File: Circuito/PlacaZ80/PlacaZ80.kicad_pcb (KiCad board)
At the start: 2 copper layers, 132.1 x 99.1 mm, 32 parts, among them J1 Conn_01x04_Pin, J2 Conn_01x14_Socket, U1 74HC00, U2 74HC138, U3 74LS08, U4 DS1233-05, U5 74HC02, U6 Z80CPU, U7 28C16, U8 6116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

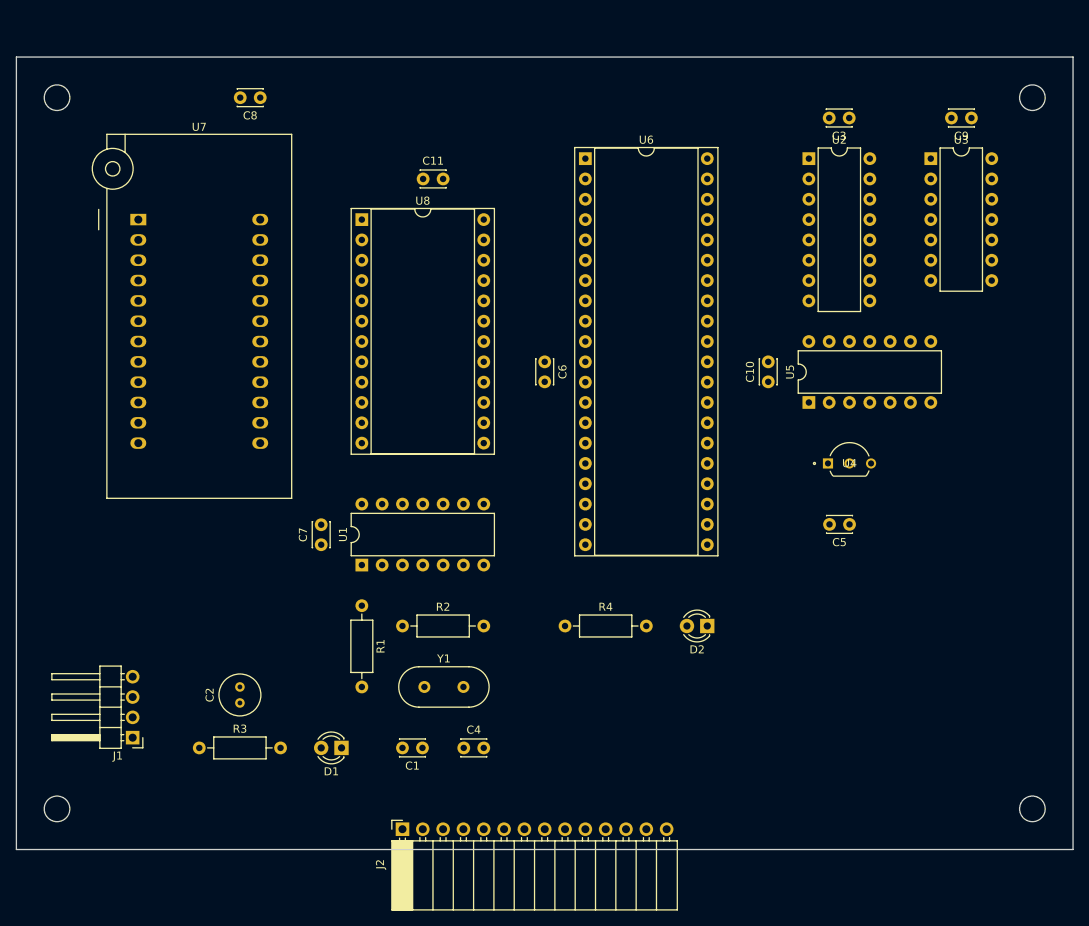
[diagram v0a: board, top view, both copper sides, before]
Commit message: Acréscimo da Placa de IO e o teste do Display
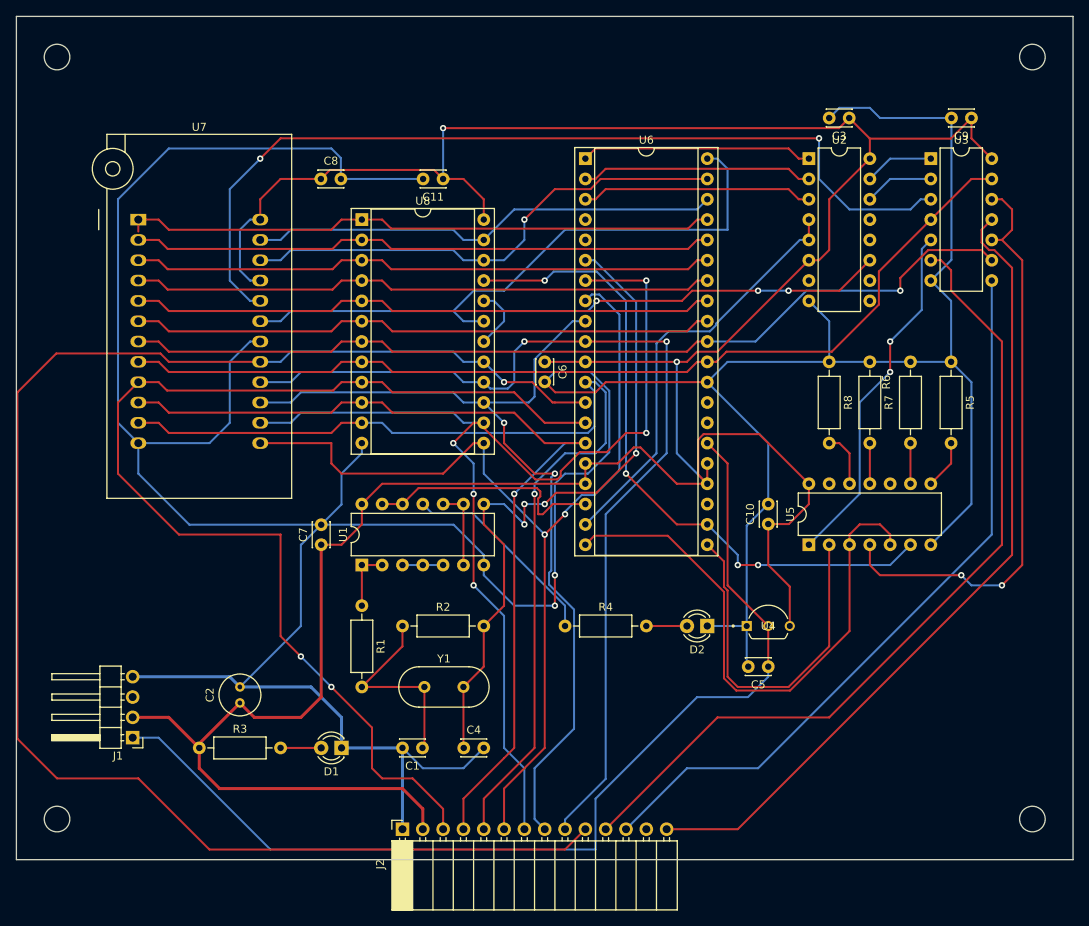
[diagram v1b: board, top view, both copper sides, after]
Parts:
- added R5: 1k, Resistor_THT:R_Axial_DIN0207_L6.3mm_D2.5mm_P10.16mm_Horizontal, F.Cu at (134.6, 58.4)
- added R6: 1k, Resistor_THT:R_Axial_DIN0207_L6.3mm_D2.5mm_P10.16mm_Horizontal, F.Cu at (129.5, 58.4)
- added R7: 1k, Resistor_THT:R_Axial_DIN0207_L6.3mm_D2.5mm_P10.16mm_Horizontal, F.Cu at (124.5, 58.4)
- added R8: 1k, Resistor_THT:R_Axial_DIN0207_L6.3mm_D2.5mm_P10.16mm_Horizontal, F.Cu at (119.4, 58.4)
- moved U4 22.7 mm to (109.1, 91.4)
- moved C5 20.5 mm to (111.8, 96.5)
- moved C10 17.8 mm to (111.8, 78.7)
- moved U5 17.8 mm to (116.8, 81.3)
- moved C8 12.7 mm to (55.8, 35.6), turned to 0 degrees
- moved REF** 5.08 mm to (144.8, 20.3)
- moved REF** 5.08 mm to (22.9, 20.3)
- moved C11 2.50 mm to (71.1, 35.6), turned to 180 degrees
- moved REF** 1.27 mm to (144.8, 115.6)
- moved REF** 1.27 mm to (22.9, 115.6)
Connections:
- U5 pad 11: unconnected-(U5-Pad11) -> Net-(R7-Pad2)
- U5 pad 12: unconnected-(U5-Pad12) -> Net-(R8-Pad2)
- U5 pad 8: unconnected-(U5-Pad8) -> Net-(R5-Pad2)
- U5 pad 9: unconnected-(U5-Pad9) -> Net-(R6-Pad2)
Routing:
- net GND: track 0.00 -> 485.8 mm, vias 0 -> 2
- net +5V: track 0.00 -> 392.3 mm, vias 0 -> 2
- net D7: track 0.00 -> 197.7 mm, vias 0 -> 1
- net D0: track 0.00 -> 142.3 mm, vias 0 -> 2
- net D4: track 0.00 -> 138.8 mm, vias 0 -> 5
- net D2: track 0.00 -> 131.2 mm, vias 0 -> 1
- net RESET: track 0.00 -> 130.3 mm
- net D3: track 0.00 -> 124.0 mm, vias 0 -> 2
- net D6: track 0.00 -> 123.1 mm, vias 0 -> 2
- net A0: track 0.00 -> 120.7 mm
- net D1: track 0.00 -> 115.1 mm, vias 0 -> 1
- net A1: track 0.00 -> 115.0 mm, vias 0 -> 1
- net ROM_OE: track 0.00 -> 113.7 mm, vias 0 -> 2
- net D5: track 0.00 -> 111.3 mm, vias 0 -> 2
- net KB_RD: track 0.00 -> 104.2 mm
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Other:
- board size 132.1 x 99.1 mm -> 132.1 x 105.4 mm
